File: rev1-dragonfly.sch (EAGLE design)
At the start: 22 parts, among them J1 USB_MINI-B_SMT, Y1 16MHz

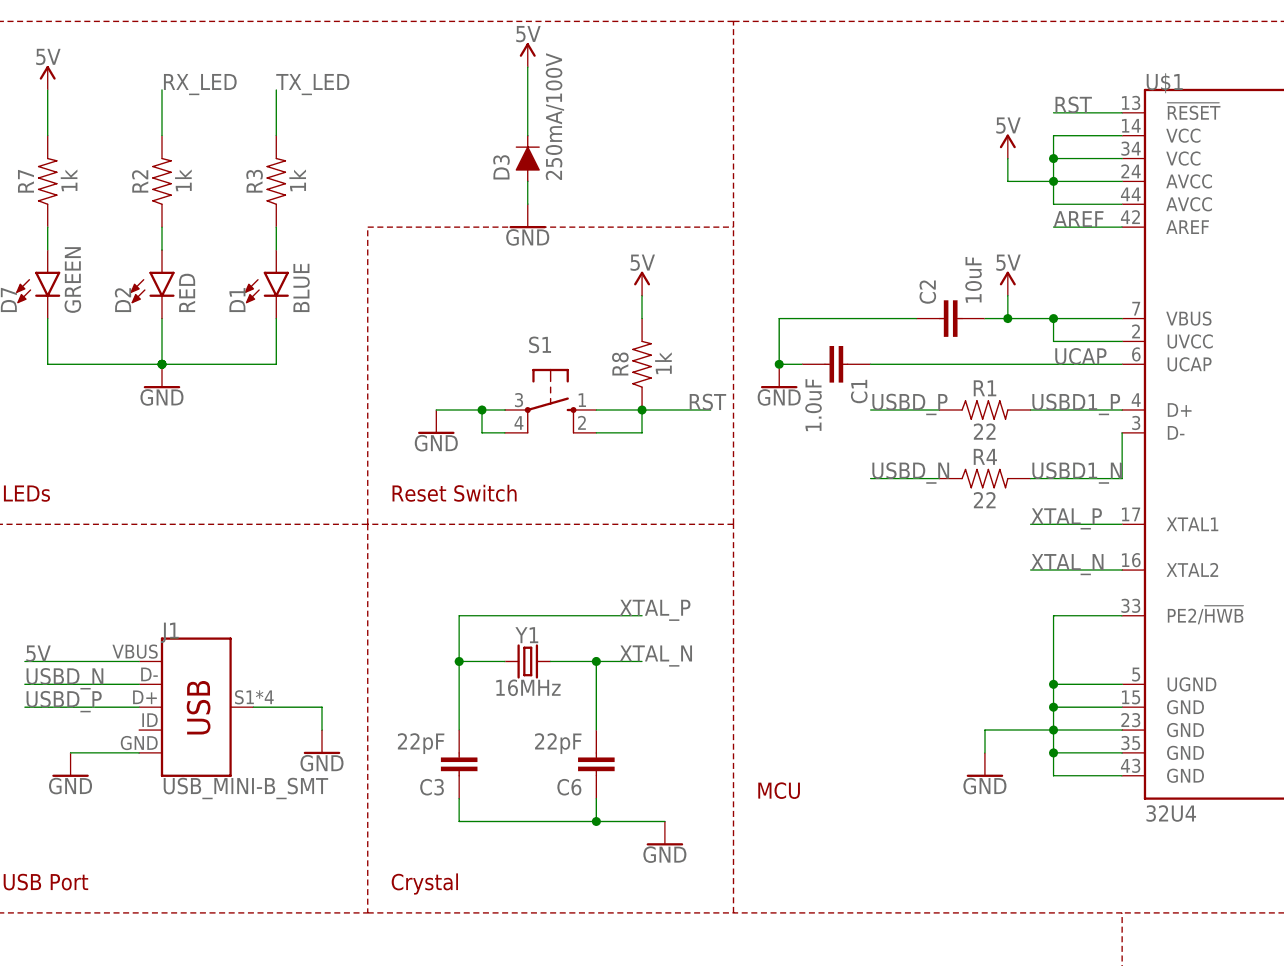
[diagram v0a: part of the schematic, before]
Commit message: Added proper eagle files
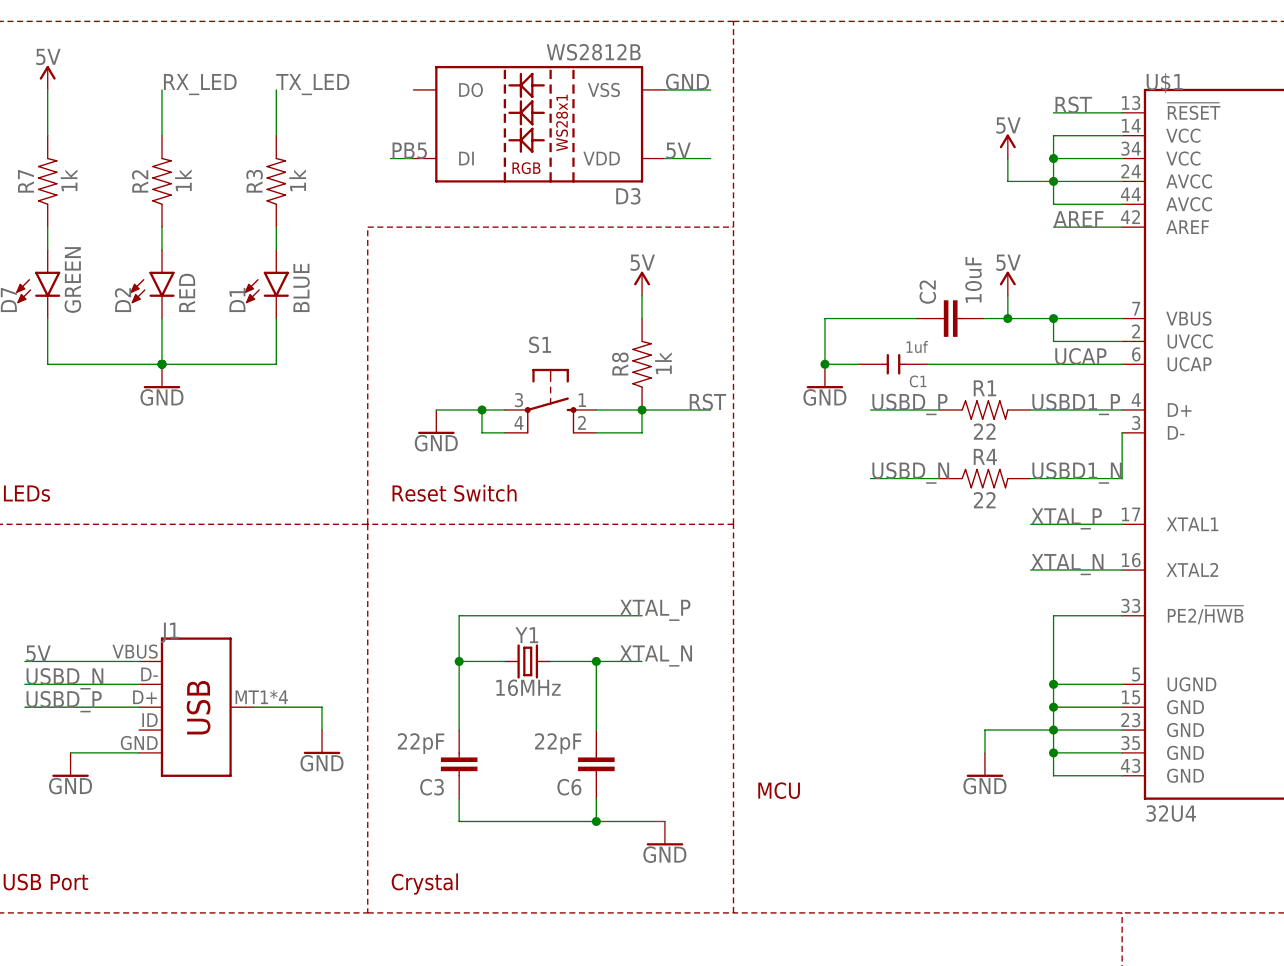
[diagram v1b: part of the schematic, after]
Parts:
- C1: value 1.0uF -> 1uf; device SparkFun-Capacitors:1.0UF-1206-50V-10% -> Seeed-Capacitor:CERAMIC-1UF-25V-10%-X7R(0603)
- C2: device SparkFun-Capacitors:10UF-1206-6.3V-20% -> SparkFun-Capacitors:10UF-0805-10V-10%
- C3, C6: device SparkFun-Capacitors:10UF-1206-6.3V-20% -> SparkFun-Capacitors:22PF-0603-50V-5%
- D1: device SparkFun-LED:LED-BLUE1206 -> SparkFun-LED:LED-BLUE0603
- D2: device SparkFun-LED:LED-RED1206 -> SparkFun-LED:LED-RED0603
- D3: value 250mA/100V -> WS2812B; device SparkFun-DiscreteSemi:DIODE-BAS16J -> SparkFun-LED:WS2812B
- D7: device SparkFun-LED:LED-GREEN1206 -> SparkFun-LED:LED-GREEN0603
- J1: value USB_MINI-B_SMT -> (none); device SparkFun-Connectors:USB_MINI-B_SMT -> SparkFun-Connectors:USB_MICRO-B_SMT
- R1, R4: value 22 -> 22; device SparkFun-Resistors:RESISTOR1206 -> SparkFun-Resistors:22OHM-0603-1/10W-1%
- R2, R7, R8: device SparkFun-Resistors:RESISTOR1206 -> SparkFun-Resistors:RESISTOR0805
- R3: value 1k -> 1k; device SparkFun-Resistors:RESISTOR1206 -> SparkFun-Resistors:RESISTOR0805
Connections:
- net 5V: now also D3.VDD; no longer D3.C
- net GND: now also D3.VSS; no longer D3.A
- net PB5: now also D3.DI
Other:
- moved on the sheet: J1
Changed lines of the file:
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@@
 <part name="ICSP" library="SparkFun-Connectors" library_urn="urn:adsk.eagle:library:513" deviceset="AVR_SPI_PRG_6" device="NS"/>
 <part name="FRAME1" library="SparkFun-Aesthetics" library_urn="urn:adsk.eagle:library:507" deviceset="FRAME-A4L" device=""/>
-<part name="D1" library="SparkFun-LED" deviceset="LED-BLUE" device="1206" value="BLUE"/>
-<part name="J1" library="SparkFun-Connectors" deviceset="USB_MINI-B" device="_SMT"/>
+<part name="D1" library="SparkFun-LED" library_urn="urn:adsk.eagle:library:529" deviceset="LED-BLUE" device="0603" value="BLUE"/>
+<part name="J1" library="SparkFun-Connectors" deviceset="USB_MICRO-B" device="_SMT"/>
 <part name="SUPPLY4" library="SparkFun-PowerSymbols" library_urn="urn:adsk.eagle:library:530" deviceset="5V" device=""/>
 <part name="SUPPLY6" library="SparkFun-PowerSymbols" library_urn="urn:adsk.eagle:library:530" deviceset="5V" device=""/>
@@
 <part name="GND7" library="SparkFun-PowerSymbols" library_urn="urn:adsk.eagle:library:530" deviceset="GND" device=""/>
 <part name="GND10" library="SparkFun-PowerSymbols" library_urn="urn:adsk.eagle:library:530" deviceset="GND" device=""/>
-<part name="R7" library="SparkFun-Resistors" deviceset="RESISTOR" device="1206" value="1k"/>
-<part name="R2" library="SparkFun-Resistors" deviceset="RESISTOR" device="1206" value="1k"/>
-<part name="R3" library="SparkFun-Resistors" deviceset="RESISTOR" device="1206" value=" 1k"/>
-<part name="R8" library="SparkFun-Resistors" deviceset="RESISTOR" device="1206" value="1k"/>
+<part name="R7" library="SparkFun-Resistors" library_urn="urn:adsk.eagle:library:532" deviceset="RESISTOR" device="0805" value="1k"/>
+<part name="R2" library="SparkFun-Resistors" library_urn="urn:adsk.eagle:library:532" deviceset="RESISTOR" device="0805" value="1k"/>
+<part name="R3" library="SparkFun-Resistors" library_urn="urn:adsk.eagle:library:532" deviceset="RESISTOR" device="0805" value="1k"/>
+<part name="R8" library="SparkFun-Resistors" library_urn="urn:adsk.eagle:library:532" deviceset="RESISTOR" device="0805" value="1k"/>
 <part name="S1" library="switch-omron" library_urn="urn:adsk.eagle:library:377" deviceset="10-XX" device=""/>
-<part name="D7" library="SparkFun-LED" deviceset="LED-GREEN" device="1206" value="GREEN"/>
+<part name="D7" library="SparkFun-LED" library_urn="urn:adsk.eagle:library:529" deviceset="LED-GREEN" device="0603" value="GREEN"/>
 <part name="SUPPLY3" library="SparkFun-PowerSymbols" library_urn="urn:adsk.eagle:library:530" deviceset="5V" device=""/>
-<part name="D2" library="SparkFun-LED" deviceset="LED-RED" device="1206" value="RED"/>
+<part name="D2" library="SparkFun-LED" library_urn="urn:adsk.eagle:library:529" deviceset="LED-RED" device="0603" value="RED"/>
 <part name="U$1" library="SparkFun-IC-Microcontroller" deviceset="ATMEGA32U4" device="TQFP-44" value="32U4"/>
-<part name="C1" library="SparkFun-Capacitors" deviceset="1.0UF" device="-1206-50V-10%" value="1.0uF"/>
-<part name="C2" library="SparkFun-Capacitors" deviceset="10UF" device="-1206-6.3V-20%" value="10uF"/>
-<part name="R1" library="SparkFun-Resistors" deviceset="RESISTOR" device="1206" value=" 22"/>
-<part name="R4" library="SparkFun-Resistors" deviceset="RESISTOR" device="1206" value=" 22"/>
+<part name="C1" library="Seeed-Capacitor" library_urn="urn:adsk.eagle:library:464" deviceset="CERAMIC-1UF-25V-10%-X7R(0603)" device="" value="1uf"/>
+<part name="C2" library="SparkFun-Capacitors" deviceset="10UF" device="-0805-10V-10%" value="10uF"/>
+<part name="R1" library="SparkFun-Resistors" deviceset="22OHM" device="-0603-1/10W-1%" value="22"/>
+<part name="R4" library="SparkFun-Resistors" deviceset="22OHM" device="-0603-1/10W-1%" value="22"/>
+<part name="D3" library="SparkFun-LED" deviceset="WS2812B" device="" value="WS2812B"/>
 <part name="Y1" library="SparkFun-Clocks" library_urn="urn:adsk.eagle:library:511" deviceset="CRYSTAL-16MHZ" device="PTH-HC49US" value="16MHz"/>
-<part name="C3" library="SparkFun-Capacitors" deviceset="10UF" device="-1206-6.3V-20%" value="22pF"/>
-<part name="C6" library="SparkFun-Capacitors" deviceset="10UF" device="-1206-6.3V-20%" value="22pF"/>
+<part name="C3" library="SparkFun-Capacitors" library_urn="urn:adsk.eagle:library:510" deviceset="22PF" device="-0603-50V-5%" value="22pF"/>
+<part name="C6" library="SparkFun-Capacitors" library_urn="urn:adsk.eagle:library:510" deviceset="22PF" device="-0603-50V-5%" value="22pF"/>
 <part name="GND1" library="SparkFun-PowerSymbols" library_urn="urn:adsk.eagle:library:530" deviceset="GND" device=""/>
 <part name="SUPPLY1" library="SparkFun-PowerSymbols" library_urn="urn:adsk.eagle:library:530" deviceset="5V" device=""/>
@@
 <part name="J2" library="SparkFun-Connectors" deviceset="CONN_03" device=""/>
 <part name="J3" library="SparkFun-Connectors" deviceset="CONN_14" device=""/>
-<part name="D3" library="SparkFun-DiscreteSemi" deviceset="DIODE" device="-BAS16J" value="250mA/100V"/>
-<part name="SUPPLY2" library="SparkFun-PowerSymbols" library_urn="urn:adsk.eagle:library:530" deviceset="5V" device=""/>
-<part name="GND4" library="SparkFun-PowerSymbols" library_urn="urn:adsk.eagle:library:530" deviceset="GND" device=""/>
 </parts>
 <sheets>
@@
 <instance part="D2" gate="G$1" x="-20.32" y="127"/>
 <instance part="U$1" gate="G$1" x="104.14" y="109.22"/>
-<instance part="C1" gate="G$1" x="53.34" y="116.84" rot="R270"/>
+<instance part="C1" gate="G$1" x="60.96" y="116.84" rot="R180"/>
 <instance part="C2" gate="G$1" x="68.58" y="121.92" rot="R90"/>
 <instance part="R1" gate="G$1" x="71.12" y="111.76"/>
 <instance part="R4" gate="G$1" x="71.12" y="104.14"/>
+<instance part="D3" gate="G$1" x="20.32" y="144.78" rot="R180"/>
 <instance part="Y1" gate="G$1" x="20.32" y="83.82"/>
 <instance part="C3" gate="G$1" x="12.7" y="73.66" rot="R180"/>
@@
 <instance part="SUPPLY1" gate="G$1" x="73.66" y="124.46"/>
 <instance part="GND2" gate="1" x="10.16" y="109.22"/>
-<instance part="GND3" gate="1" x="48.26" y="114.3"/>
+<instance part="GND3" gate="1" x="53.34" y="114.3"/>
 <instance part="J4" gate="G$1" x="172.72" y="99.06" rot="R180"/>
 <instance part="J2" gate="J$1" x="175.26" y="81.28" rot="R180"/>
 <instance part="J3" gate="G$1" x="205.74" y="88.9" rot="R180"/>
-<instance part="D3" gate="G$1" x="20.32" y="139.7" rot="R90"/>
-<instance part="SUPPLY2" gate="G$1" x="20.32" y="149.86"/>
-<instance part="GND4" gate="1" x="20.32" y="132.08"/>
 </instances>
 <busses>
@@
 </segment>
 <segment>
+<pinref part="D3" gate="G$1" pin="VSS"/>
+<wire x1="35.56" y1="147.32" x2="40.64" y2="147.32" width="0.1524" layer="91"/>
+<label x="35.56" y="147.32" size="1.778" layer="95"/>
+</segment>
+<segment>
 <pinref part="S1" gate="1" pin="P"/>
 <wire x1="17.78" y1="111.76" x2="15.24" y2="111.76" width="0.1524" layer="91"/>
@@
 <pinref part="GND3" gate="1" pin="GND"/>
 <pinref part="C1" gate="G$1" pin="2"/>
-<wire x1="50.8" y1="116.84" x2="48.26" y2="116.84" width="0.1524" layer="91"/>
-<junction x="48.26" y="116.84"/>
-<wire x1="48.26" y1="116.84" x2="48.26" y2="121.92" width="0.1524" layer="91"/>
-<wire x1="48.26" y1="121.92" x2="63.5" y2="121.92" width="0.1524" layer="91"/>
-</segment>
-<segment>
-<pinref part="D3" gate="G$1" pin="A"/>
-<pinref part="GND4" gate="1" pin="GND"/>
-<wire x1="20.32" y1="137.16" x2="20.32" y2="134.62" width="0.1524" layer="91"/>
+<wire x1="57.15" y1="116.84" x2="53.34" y2="116.84" width="0.1524" layer="91"/>
+<junction x="53.34" y="116.84"/>
+<wire x1="53.34" y1="116.84" x2="53.34" y2="121.92" width="0.1524" layer="91"/>
+<wire x1="53.34" y1="121.92" x2="63.5" y2="121.92" width="0.1524" layer="91"/>
 </segment>
 </net>
@@
 </segment>
 <segment>
+<pinref part="D3" gate="G$1" pin="VDD"/>
+<wire x1="35.56" y1="139.7" x2="40.64" y2="139.7" width="0.1524" layer="91"/>
+<label x="35.56" y="139.7" size="1.778" layer="95"/>
+</segment>
+<segment>
 <pinref part="C2" gate="G$1" pin="2"/>
 <wire x1="78.74" y1="121.92" x2="73.66" y2="121.92" width="0.1524" layer="91"/>
@@
 <junction x="73.66" y="121.92"/>
 </segment>
-<segment>
-<wire x1="20.32" y1="142.24" x2="20.32" y2="149.86" width="0.1524" layer="91"/>
-<pinref part="SUPPLY2" gate="G$1" pin="5V"/>
-<pinref part="D3" gate="G$1" pin="C"/>
-</segment>
 </net>
 <net name="USBD_P" class="0">
@@
 <segment>
 <pinref part="U$1" gate="G$1" pin="UCAP"/>
-<wire x1="86.36" y1="116.84" x2="58.42" y2="116.84" width="0.1524" layer="91"/>
+<wire x1="86.36" y1="116.84" x2="64.77" y2="116.84" width="0.1524" layer="91"/>
 <label x="78.74" y="116.84" size="1.778" layer="95"/>
 <pinref part="C1" gate="G$1" pin="1"/>
@@
 </segment>
 <segment>
+<pinref part="D3" gate="G$1" pin="DI"/>
+<wire x1="7.62" y1="139.7" x2="5.08" y2="139.7" width="0.1524" layer="91"/>
+<label x="5.08" y="139.7" size="1.778" layer="95"/>
+</segment>
+<segment>
 <wire x1="195.58" y1="104.14" x2="185.42" y2="104.14" width="0.1524" layer="91"/>
 <label x="185.42" y="104.14" size="1.778" layer="95"/>
@@
 </sheet>
 </sheets>
+<errors>
+</errors>
 </schematic>
 </drawing>
